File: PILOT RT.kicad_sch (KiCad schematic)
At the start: 30 parts, among them J15 Conn_01x03, J16 Conn_01x03, J17 Conn_01x03, J18 Conn_01x03, J19 Conn_01x03, J20 USB_B_Micro, SW3 SW_SPDT, U5 STM32F103C8T6, U6 USBLC6-2SC6, Y2 8MHz

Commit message: first wiring
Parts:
- C32, C33: footprint Capacitor_SMD:C_0603_1608Metric -> Capacitor_SMD:C_0402_1005Metric
- D2: footprint Capacitor_SMD:C_0201_0603Metric -> Diode_SMD:D_0603_1608Metric
- R33: footprint Resistor_SMD:R_0201_0603Metric -> Resistor_SMD:R_0603_1608Metric
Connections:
- net +3.3VA: no longer C30.1, C31.1, L2.2
- new net +3.3VA_2: C30.1, C31.1, L2.2
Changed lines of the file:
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@@
 			)
 		)
-		(property "Footprint" "Capacitor_SMD:C_0603_1608Metric"
+		(property "Footprint" "Capacitor_SMD:C_0402_1005Metric"
 			(at 162.56 19.05 0)
 			(effects
@@
 			)
 		)
-		(property "Footprint" "Capacitor_SMD:C_0603_1608Metric"
+		(property "Footprint" "Capacitor_SMD:C_0402_1005Metric"
 			(at 162.56 26.67 0)
 			(effects
@@
 			)
 		)
-		(property "Footprint" "Resistor_SMD:R_0201_0603Metric"
+		(property "Footprint" "Resistor_SMD:R_0603_1608Metric"
 			(at 259.08 24.13 0)
 			(effects
@@
 			)
 		)
-		(property "Value" "+3.3VA"
+		(property "Value" "+3.3VA_2"
 			(at 147.32 16.51 0)
 			(effects
@@
 			)
 		)
-		(property "Footprint" "Capacitor_SMD:C_0201_0603Metric"
+		(property "Footprint" "Diode_SMD:D_0603_1608Metric"
 			(at 251.46 24.13 0)
 			(effects

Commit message: gerber files
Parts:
- C24, C26, C27, C28, C29: LCSC Part # (none) -> C1525
- C25: LCSC Part # (none) -> C19666
- C30: LCSC Part # (none) -> C77006
- C31: LCSC Part # (none) -> C15195
- C32, C33: LCSC Part # (none) -> C1658
- D2: LCSC Part # (none) -> C2286
- J15: LCSC Part # (none) -> C489717
- J16, J17, J18, J19: LCSC Part # (none) -> C161691
- J20: LCSC Part # (none) -> C114094
- L2: LCSC Part # (none) -> C408157
- R26, R27, R31: LCSC Part # (none) -> C25744
- R28, R29: LCSC Part # (none) -> C25092
- R30: LCSC Part # (none) -> C25867
- R32: LCSC Part # (none) -> C17168
- R33: LCSC Part # (none) -> C21190
- SW3: LCSC Part # (none) -> C778186
- U5: LCSC Part # (none) -> C8734
- U6: LCSC Part # (none) -> C2827654
- Y2: LCSC Part # (none) -> C115962
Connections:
- net +3.3VA_2 is gone; now on net 3.3VA_2: C30.1, C31.1, L2.2
- net +3.3VA renamed 3.3VA_2

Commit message: fix wrong footprints
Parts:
- C32, C33: footprint Capacitor_SMD:C_0402_1005Metric -> Capacitor_SMD:C_0603_1608Metric
- J20: footprint Connector_USB:USB_Micro-B_Molex-105017-0001 -> kwrzesni:USB-B micro
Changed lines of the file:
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@@
 			)
 		)
-		(property "Footprint" "Capacitor_SMD:C_0402_1005Metric"
+		(property "Footprint" "Capacitor_SMD:C_0603_1608Metric"
 			(at 162.56 19.05 0)
 			(effects
@@
 			)
 		)
-		(property "Footprint" "Capacitor_SMD:C_0402_1005Metric"
+		(property "Footprint" "Capacitor_SMD:C_0603_1608Metric"
 			(at 162.56 26.67 0)
 			(effects
@@
 			)
 		)
-		(property "Footprint" "Connector_USB:USB_Micro-B_Molex-105017-0001"
+		(property "Footprint" "kwrzesni:USB-B micro"
 			(at 260.35 106.68 0)
 			(effects

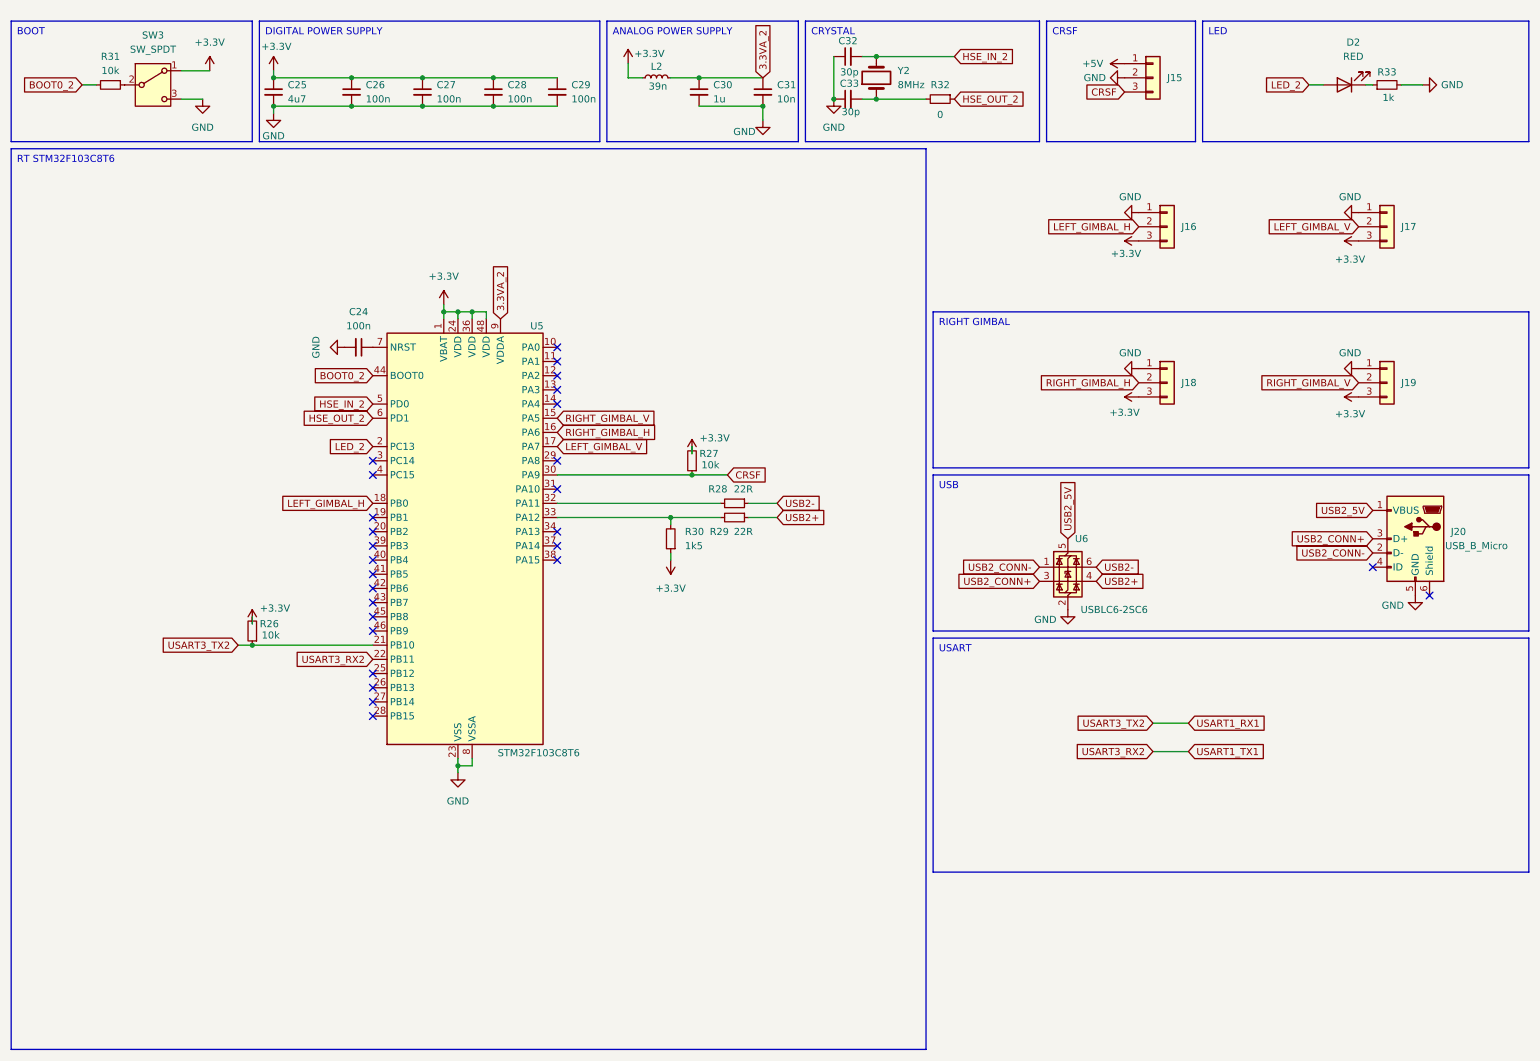
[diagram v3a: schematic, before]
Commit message: update to STM32F04
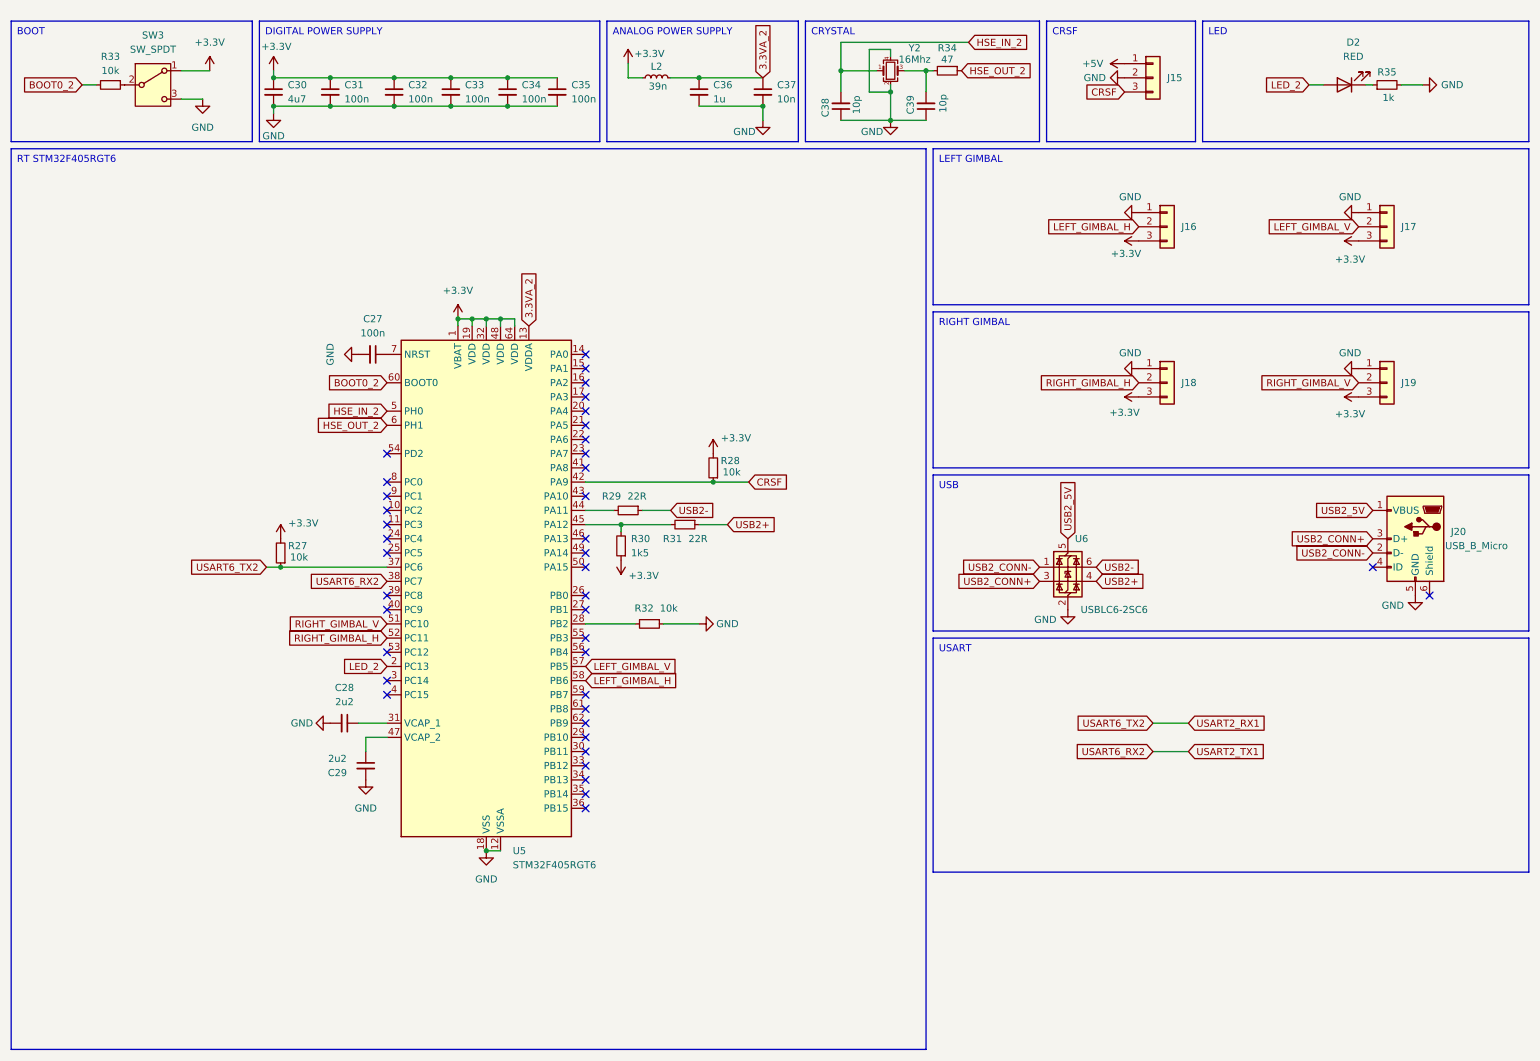
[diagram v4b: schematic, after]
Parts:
- removed C24, C26: 100n, Capacitor_SMD:C_0402_1005Metric, symbol Device:C_Small
- removed C25: 4u7, Capacitor_SMD:C_0603_1608Metric, symbol Device:C_Small
- removed R26: 10k, Resistor_SMD:R_0402_1005Metric, symbol Device:R_Small
- removed U5: STM32F103C8T6, Package_QFP:LQFP-48_7x7mm_P0.5mm, symbol MCU_ST_STM32F1:STM32F103C8Tx
- removed Y2: 8MHz, Crystal:Crystal_SMD_5032-2Pin_5.0x3.2mm, symbol Device:Crystal
- added C30: 4u7, Capacitor_SMD:C_0603_1608Metric, symbol Device:C_Small
- added C31, C34, C35: 100n, Capacitor_SMD:C_0402_1005Metric, symbol Device:C_Small
- added C38, C39: 10p, Capacitor_SMD:C_0402_1005Metric, symbol Device:C_Small
- added R31: 22R, Resistor_SMD:R_0402_1005Metric, symbol Device:R_Small
- added R34: 47, Resistor_SMD:R_0402_1005Metric, symbol Device:R_Small
- added U5: STM32F405RGT6, Package_QFP:LQFP-64_10x10mm_P0.5mm, symbol MCU_ST_STM32F4:STM32F405RGTx
- added Y2: 16Mhz, Crystal:Crystal_SMD_3225-4Pin_3.2x2.5mm, symbol Device:Crystal_GND24_Small
- C28, C29: value 100n -> 2u2; footprint Capacitor_SMD:C_0402_1005Metric -> Capacitor_SMD:C_0603_1608Metric; LCSC Part # C1525 -> C466784
- C32, C33: value 30p -> 100n; footprint Capacitor_SMD:C_0603_1608Metric -> Capacitor_SMD:C_0402_1005Metric; LCSC Part # C1658 -> C1525
- R28: value 22R -> 10k; LCSC Part # C25092 -> C25744
- R32: value 0 -> 10k; LCSC Part # C17168 -> C25092
- renumbered C30 to C36, C31 to C37, R31 to R33, R33 to R35
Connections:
- net +3.3V: now also C32.1, C33.1, R28.2, C30.1, C31.1, C34.1, C35.1, U5.1 (VBAT), U5.19 (VDD), U5.32 (VDD), U5.48 (VDD), U5.64 (VDD); no longer C27.1, C28.1, C29.1
- net 3.3VA_2: now also U5.13 (VDDA)
- net BOOT0_2: now also U5.60 (BOOT0)
- net CRSF: now also R28.1, U5.42 (PA9); no longer R27.1
- net GND: now also C32.2, C33.2, R32.1, C30.2, C31.2, C34.2, C35.2, C38.1, C39.1, U5.12 (VSSA), U5.18 (VSS), U5.63 (VSS), Y2.2, Y2.4; no longer C32.1, C33.1
- net HSE_IN_2: now also C38.2, U5.5 (PH0), Y2.1; no longer C32.2
- net HSE_OUT_2: now also R34.1, U5.6 (PH1); no longer R32.1
- net LED_2: now also U5.2 (PC13)
- net LEFT_GIMBAL_H: now also U5.58 (PB6)
- net LEFT_GIMBAL_V: now also U5.57 (PB5)
- net RIGHT_GIMBAL_H: now also U5.52 (PC11)
- net RIGHT_GIMBAL_V: now also U5.51 (PC10)
- net USB2+: now also R31.1; no longer R29.1
- net USB2-: now also R29.1; no longer R28.1
- net at R29.2: now also U5.44 (PA11); no longer R30.2
- net at R32.2: now also U5.28 (PB2); no longer C33.2
- new net: C39.2, R34.2, Y2.3
- new net: C29.1, U5.47 (VCAP_2)
- new net: R30.2, R31.2, U5.45 (PA12)
- new net: C28.1, U5.31 (VCAP_1)
- new net: C27.1, U5.7 (NRST)
- new net USART2_RX1: R27.1, U5.37 (PC6)
- new net USART2_TX1: U5.38 (PC7)
- no-connect marks 27 -> 40
